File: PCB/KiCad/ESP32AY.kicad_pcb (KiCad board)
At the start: 2 copper layers, 55 x 100 mm, 109 parts, among them J1 ZX62D-B-5P8, J2 MiniJack, J3 SD Card, Q1 BC807, Q2 BC817, Q3 BC817, SW1 SW_Push, SW2 EN, SW3 BOOT, U1 AY-3-8910, U2 AY-3-8910, U3 CH340G, U4 ESP32-WROOM-32, U5 TPA6130A2RTJTG4, U6 SM5308, U7 AMS1117-3.3, U8 74HC595, U9 74HC595, Y3 12MHz

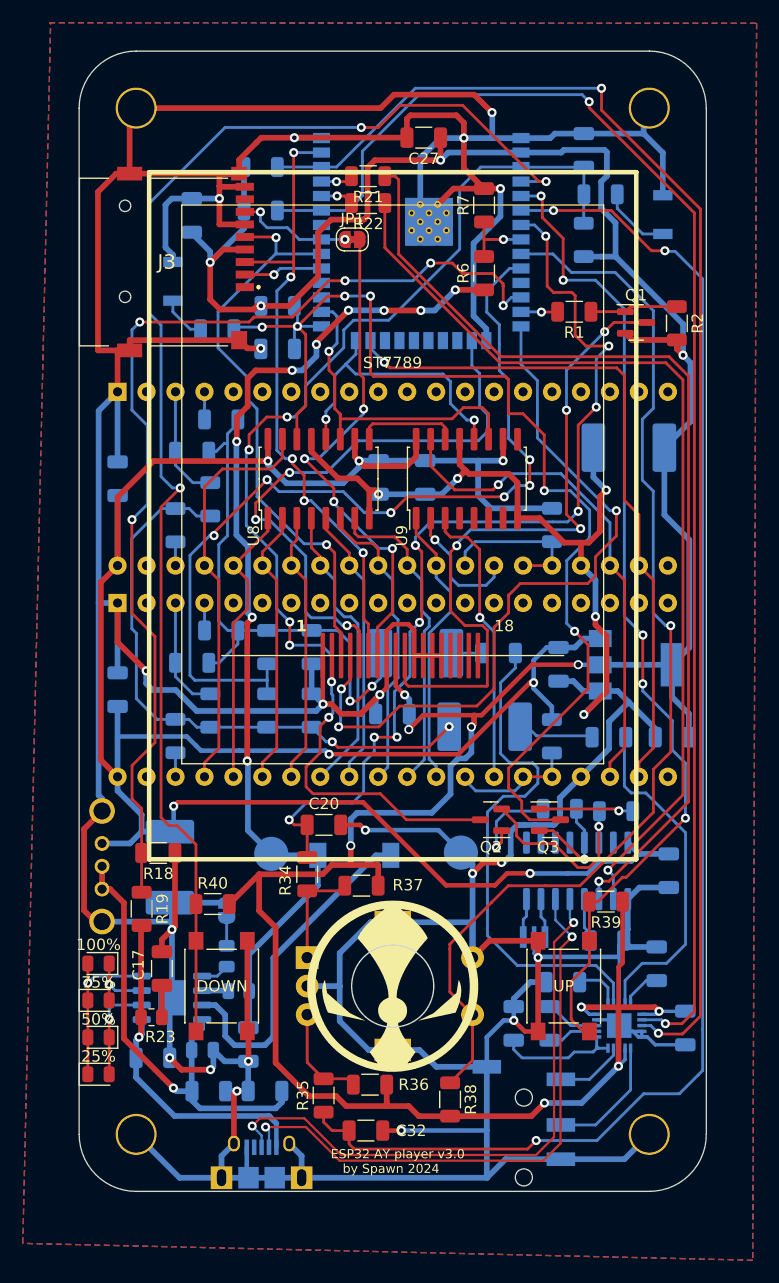
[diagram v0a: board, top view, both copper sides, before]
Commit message: PCB Rev. B (Type-C and Stereo DAC)
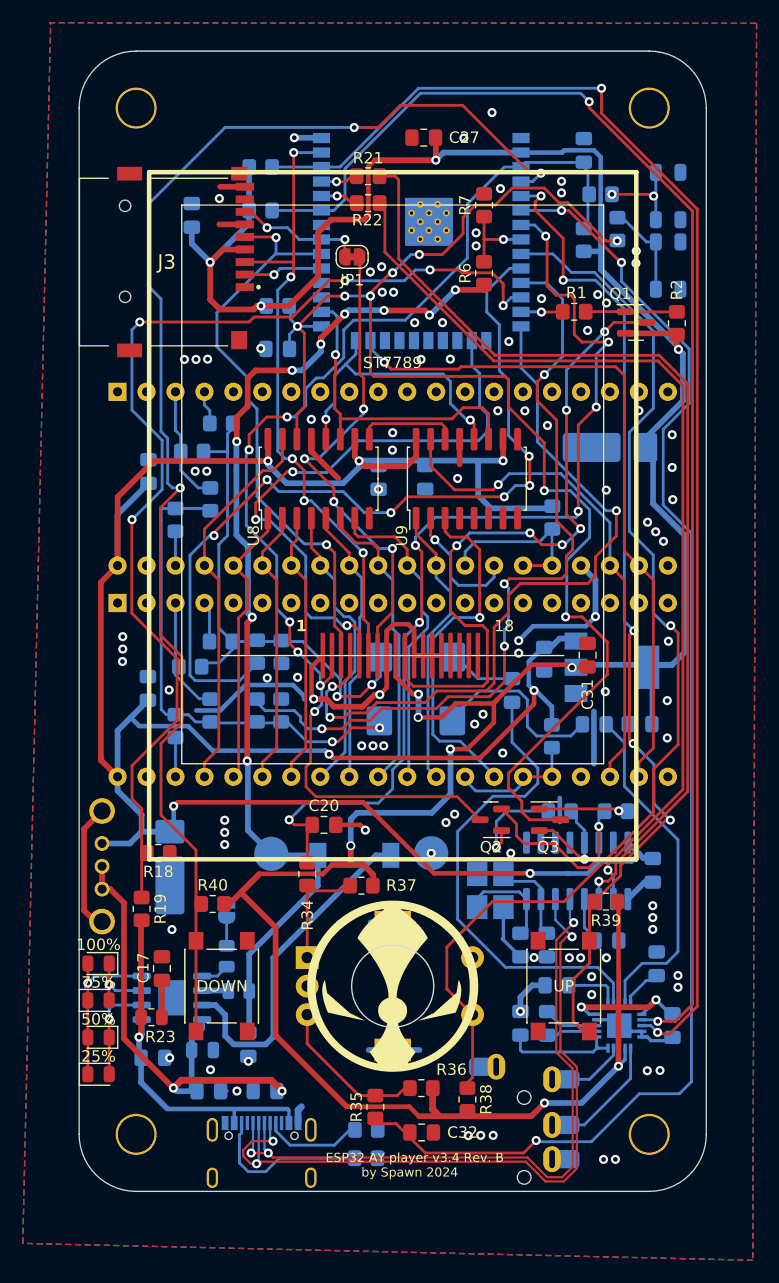
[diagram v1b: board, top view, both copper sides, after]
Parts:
- added C33: 22, Capacitor_SMD:C_0805_2012Metric_Pad1.18x1.45mm_HandSolder, B.Cu at (61.0, 98.4)
- added C34: 22, Capacitor_SMD:C_0805_2012Metric_Pad1.18x1.45mm_HandSolder, B.Cu at (58.7, 98.4)
- added R41: 5K1, Resistor_SMD:R_0805_2012Metric_Pad1.20x1.40mm_HandSolder, B.Cu at (45.2, 114.6)
- added R42: 5K1, Resistor_SMD:R_0805_2012Metric_Pad1.20x1.40mm_HandSolder, B.Cu at (45.2, 117.1)
- C1, C10, C11, C12, C13, C14, C16, C17, C18, C19, C2, C20, C21, C22, C24, C26, C27, C28, C29, C3, C30, C32, C5, C6, C7, C8: footprint Capacitor_SMD:C_1206_3216Metric -> Capacitor_SMD:C_0805_2012Metric_Pad1.18x1.45mm_HandSolder
- C15, C9: footprint Capacitor_Tantalum_SMD:CP_EIA-7360-38_Kemet-E -> Capacitor_Tantalum_SMD:CP_EIA-7343-31_Kemet-D_Pad2.25x2.55mm_HandSolder
- C25, C4: footprint Capacitor_Tantalum_SMD:CP_EIA-7360-38_Kemet-E -> footprints:CP_EIA-7343-31_Kemet-D-uni
- C31: footprint Capacitor_SMD:C_1206_3216Metric -> Capacitor_SMD:C_0805_2012Metric_Pad1.18x1.45mm_HandSolder; moved to F.Cu
- J1: value ZX62D-B-5P8 -> USB_C_Receptacle_USB2.0_14P; footprint mod:HRS_ZX62D-B-5P8 -> Connector_USB:USB_C_Receptacle_G-Switch_GT-USB-7010ASV
- J2: footprint mod:Jack_3.5mm_PJ320D_Horizontal -> footprints:AUDIO_JACK_3.5MM_SMD_TRRS_rounded_mixed
- R1, R10, R11, R12, R13, R14, R15, R16, R17, R18, R19, R2, R20, R21, R22, R26, R27, R29, R3, R31, R34, R35, R36, R37, R38, R39, R4, R40, R5, R6, R7, R8, R9: footprint Resistor_SMD:R_1206_3216Metric -> Resistor_SMD:R_0805_2012Metric_Pad1.20x1.40mm_HandSolder
- R28, R30: value 470 -> 10K; footprint Resistor_SMD:R_1206_3216Metric -> Resistor_SMD:R_0805_2012Metric_Pad1.20x1.40mm_HandSolder
- R32, R33: value 5.6K -> 1K; footprint Resistor_SMD:R_1206_3216Metric -> Resistor_SMD:R_0805_2012Metric_Pad1.20x1.40mm_HandSolder
- SW2, SW3: footprint Button_Switch_SMD:SW_SPST_B3U-1000P -> footprints:SW_SPST_PTS810_handsoldering
- Y3: footprint mod:OSC_CSTCE16M0V53-R0 -> Crystal:Crystal_SMD_3225-4Pin_3.2x2.5mm_HandSoldering
- moved SW3 43.5 mm to (71.7, 38.8), turned to 90 degrees
- moved R31 36.2 mm to (67.2, 35.6), turned to 90 degrees
- moved C31 17.9 mm to (64.6, 73.0), turned to -90 degrees
- moved J2 6.37 mm to (59.0, 120.4)
- moved C15 6.05 mm to (49.5, 78.7)
- moved Y3 5.60 mm to (56.1, 93.6), turned to -90 degrees
- moved C32 4.89 mm to (50.0, 114.8)
- moved R35 4.64 mm to (46.0, 112.6)
- moved R36 4.51 mm to (50.0, 110.9)
- moved C13 3.49 mm to (58.0, 76.1), turned to 90 degrees
- moved C24 3.04 mm to (69.2, 79.0)
- moved C2 2.79 mm to (26.1, 56.9)
- moved R8 2.68 mm to (37.7, 72.7)
- moved R13 2.67 mm to (37.7, 77.8)
- moved C1 2.67 mm to (26.0, 75.9)
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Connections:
- Encoder1 pad MP: GND -> (no net)
- R32 pad 2: DAC_SOUND -> DAC_SOUND_L
- R33 pad 2: DAC_SOUND -> DAC_SOUND_R
- S6 pad P$4: GND -> (no net)
- S6 pad P$5: GND -> (no net)
- U4 pad 10: DAC_SOUND -> DAC_SOUND_L
- U4 pad 11: unconnected-(U4-DAC2/IO26-Pad11) -> DAC_SOUND_R
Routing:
- net GND: track 685.3 -> 122.2 mm, vias 25 -> 99
- net DAC_SOUND: track 77.4 -> 0.00 mm, vias 6 -> 0
- net DAC_SOUND_L: track 0.00 -> 74.6 mm, vias 0 -> 6
- net DAC_SOUND_R: track 0.00 -> 70.4 mm, vias 0 -> 4
- net 595_DATA: track 100.5 -> 125.2 mm, vias 6 -> 8
- net Net-(J1-CC2): track 0.00 -> 14.0 mm
- net UD-: track 52.1 -> 65.5 mm, vias 2 -> 3
- net MIX_R: track 6.69 -> 16.1 mm
- net AYMIX_R: track 52.4 -> 43.5 mm
- net Net-(J1-CC1): track 0.00 -> 8.25 mm
- net ENC_B: track 126.5 -> 118.4 mm
- net UD+: track 52.6 -> 60.0 mm, vias 2 -> 3
- net AY2_BDIR: track 25.3 -> 31.1 mm
- net Net-(U3-XO): track 3.45 -> 8.81 mm
- net Net-(U3-XI): track 3.47 -> 7.98 mm
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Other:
- board text added: "ESP32 AY player v3.4 Rev. B by Spawn 2024"
- board text removed: "ESP32 AY player v3.0 by Spawn 2024"

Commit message: Release 3.4 (added mod+s3m formats), LCD moved to dedicated SPI with revision C PCB or soldering upgrade from revision A and B to revision C (see README). Some optimizations and new features.
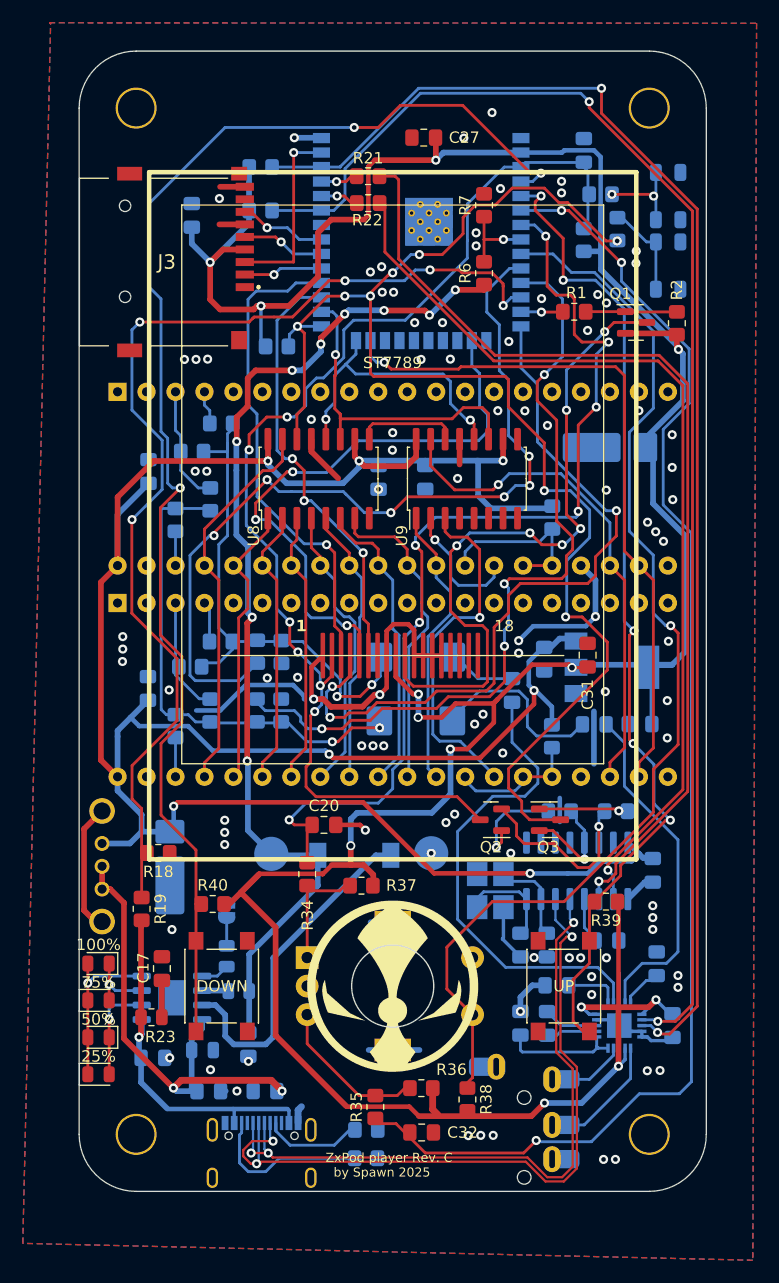
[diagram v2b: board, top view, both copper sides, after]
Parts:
- removed C30: 100n, Capacitor_SMD:C_0805_2012Metric_Pad1.18x1.45mm_HandSolder
- removed JP1: jumper, Jumper:SolderJumper-2_P1.3mm_Bridged_RoundedPad1.0x1.5mm
- R7: value 10K -> 20K
- moved R30 3.55 mm to (37.4, 45.9)
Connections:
- TFT1 pad 3: SPI_CLK -> TFT_CLK
- TFT1 pad 6: SPI_MOSI -> TFT_MOSI
- TFT1 pad 7: Net-(JP1-B) -> unconnected-(TFT1-SDO(MISO)-Pad7)
- U4 pad 27: unconnected-(U4-IO16-Pad27) -> TFT_MOSI
- U4 pad 28: unconnected-(U4-IO17-Pad28) -> TFT_CLK
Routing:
- net SPI_CLK: track 51.2 -> 7.34 mm, vias 2 -> 1
- net TFT_CLK: track 0.00 -> 42.8 mm, vias 0 -> 1
- net Net-(JP1-B): track 42.4 -> 0.00 mm, vias 4 -> 0
- net SPI_MOSI: track 55.4 -> 16.3 mm, vias 5 -> 1
- net TFT_MOSI: track 0.00 -> 38.2 mm, vias 0 -> 3
- net +3.3V: track 288.1 -> 291.9 mm
- net SPI_MISO: track 11.3 -> 7.72 mm, vias 2 -> 1
- net 595_DATA: track 125.2 -> 123.0 mm
- net GND: track 122.2 -> 122.1 mm, vias 99 -> 98
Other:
- board text added: "ZxPod player Rev. C by Spawn 2025"
- board text removed: "ESP32 AY player v3.4 Rev. B by Spawn 2024"

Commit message: Refactored schematics, updated BOM
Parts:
- C33, C34: value 22 -> 22p
- R24: value R50 -> 0.5R
- SW1: value SW_Push -> Check bat
- U6: value SM5308 -> IP5306
- turned C28 to -90 degrees
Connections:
- C28 pad 1: +3.3V -> GND
- C28 pad 2: GND -> +3.3V

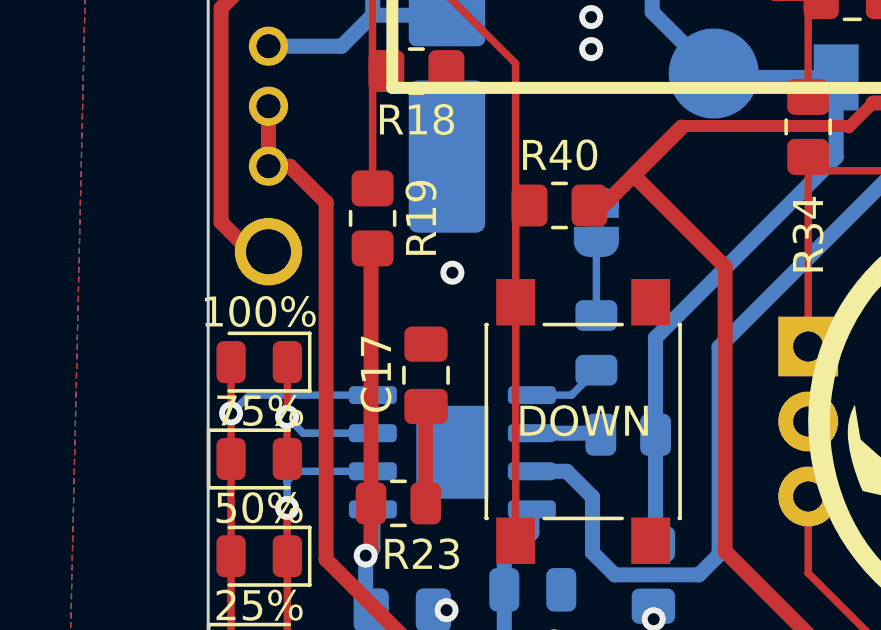
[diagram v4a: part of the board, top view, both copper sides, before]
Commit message: Added C30 to the charger unit
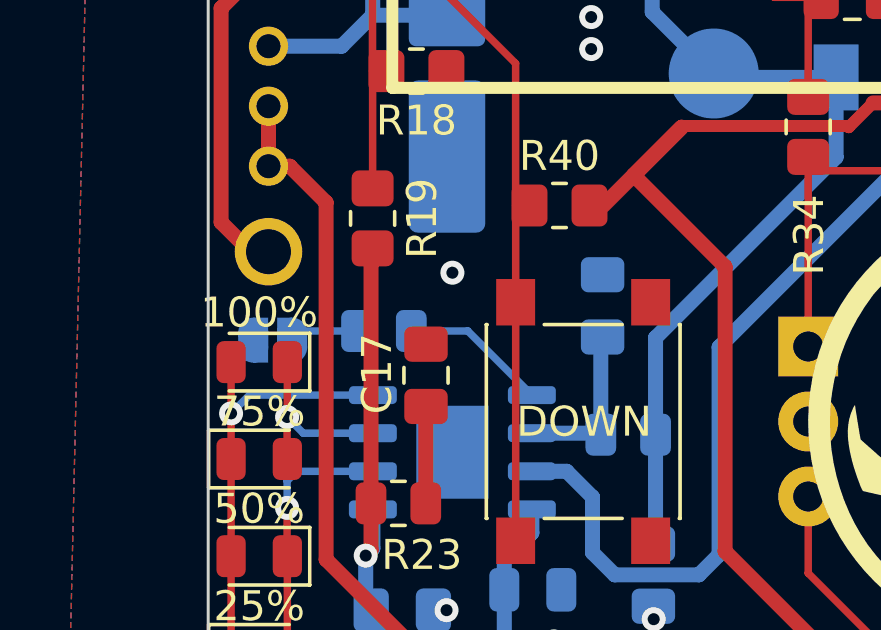
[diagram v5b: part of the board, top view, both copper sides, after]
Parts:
- added C30: 22uf, Capacitor_SMD:C_0805_2012Metric_Pad1.18x1.45mm_HandSolder, B.Cu at (33.1, 98.1)
- R23: value 0.1R -> 2R
- moved SW1 11.5 mm to (22.1, 99.3), turned to 0 degrees
- moved R25 7.09 mm to (25.9, 99.0), turned to 180 degrees
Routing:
- net Net-(U6-BAT): track 2.32 -> 5.60 mm
- net Net-(U6-KEY): track 2.49 -> 4.91 mm

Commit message: Fixed R7 from 20k to 10k
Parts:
- R7: value 20K -> 10K
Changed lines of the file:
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@@
 			)
 		)
-		(property "Value" "20K"
+		(property "Value" "10K"
 			(at 0 1.65 90)
 			(layer "F.Fab")

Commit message: Schematics change: replaced R19 from 0 to 8K2
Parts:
- R19: value 0 -> 8,2К*
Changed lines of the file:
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@@
 			)
 		)
-		(property "Value" "0"
+		(property "Value" "8,2К*"
 			(at 0 1.65 270)
 			(layer "F.Fab")

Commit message: RevC1 - initial commit
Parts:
- added C35: 100n, Capacitor_SMD:C_0805_2012Metric_Pad1.18x1.45mm_HandSolder, B.Cu at (35.9, 34.4)
- added C36: 100n, Capacitor_SMD:C_0805_2012Metric_Pad1.18x1.45mm_HandSolder, B.Cu at (26.8, 41.8)
- added U10: DS3231MZ, Package_SO:SOIC-8_3.9x4.9mm_P1.27mm, B.Cu at (28.5, 37.1)
- added U11: 24LC256, Package_SO:SOIC-8_3.9x4.9mm_P1.27mm, B.Cu at (28.5, 31.5)
- C17, C27, R1: moved to B.Cu
- C19, C21, C22, C30: footprint Capacitor_SMD:C_0805_2012Metric_Pad1.18x1.45mm_HandSolder -> Capacitor_SMD:C_1206_3216Metric_Pad1.33x1.80mm_HandSolder
- C23: footprint Capacitor_SMD:C_0805_2012Metric -> Capacitor_SMD:C_1206_3216Metric_Pad1.33x1.80mm_HandSolder
- R23: footprint Resistor_SMD:R_0805_2012Metric -> Resistor_SMD:R_0805_2012Metric_Pad1.20x1.40mm_HandSolder; moved to B.Cu
- R31: moved to F.Cu
- U3: value CH340G -> CH340C
- U8, U9: footprint Package_SO:SO-16_5.3x10.2mm_P1.27mm -> Package_SO:SO-16_3.9x9.9mm_P1.27mm
- moved R21 65.4 mm to (72.3, 90.6), turned to 90 degrees
- moved R22 62.4 mm to (70.3, 90.6), turned to 90 degrees
- moved L1 18.6 mm to (28.4, 100.4)
- moved C30 15.5 mm to (24.3, 110.9), turned to 0 degrees
- moved C17 14.8 mm to (38.4, 110.1), turned to 90 degrees
- moved C22 12.5 mm to (36.8, 99.9), turned to 90 degrees
- moved C27 12.0 mm to (62.1, 28.7), turned to 90 degrees
- moved R23 11.3 mm to (36.2, 110.1), turned to 90 degrees
- moved R6 11.1 mm to (59.3, 29.1), turned to 0 degrees
- moved R24 10.8 mm to (25.1, 108.6)
- moved C19 10.6 mm to (24.3, 106.2), turned to 0 degrees
- moved R7 9.54 mm to (63.9, 29.0), turned to 0 degrees
- moved BAT-1 7.88 mm to (43.2, 91.9)
- moved C18 7.84 mm to (34.1, 110.1), turned to -90 degrees
- moved Q3 7.20 mm to (57.5, 93.5), turned to -90 degrees
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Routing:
- net Net-(U4-TXD0/IO1): track 2.83 -> 81.4 mm
- net TX0: track 87.1 -> 8.95 mm
- net Net-(U4-RXD0/IO3): track 2.89 -> 80.4 mm
- net RX0: track 83.2 -> 6.68 mm
- net Bat+: track 90.5 -> 127.8 mm, vias 9 -> 12
- net Net-(U6-SW): track 30.0 -> 5.70 mm
- net SDA: track 121.5 -> 143.6 mm, vias 2 -> 4
- net SCL: track 121.5 -> 135.8 mm
- net Net-(U6-Vout): track 41.1 -> 29.3 mm, vias 2 -> 3
- net Vin: track 31.9 -> 43.0 mm, vias 1 -> 3
- net BT_DN: track 120.1 -> 130.8 mm, vias 3 -> 7
- net Net-(D3-A): track 6.32 -> 16.5 mm
- net Net-(Q1-B): track 7.55 -> 17.7 mm, vias 0 -> 1
- net TFT_LED: track 59.9 -> 68.9 mm
- net +3.3V: track 291.9 -> 283.4 mm, vias 13 -> 14
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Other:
- board text added: "LiPo Battery 2000 mAh"
- board text added: "ZxPod player Rev. C1 by Spawn 2025"
- board text removed: "ZxPod player Rev. C by Spawn 2025"
